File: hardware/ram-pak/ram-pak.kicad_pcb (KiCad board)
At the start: 4 copper layers, 29 x 16.7 mm, 29 parts, among them J1 PinHeader_2x22_P1.27mm, J2 pkl_jumper, U1 TLV62568DBV, U2 W957D8MFYA5I, U3 W957D8MFYA5I

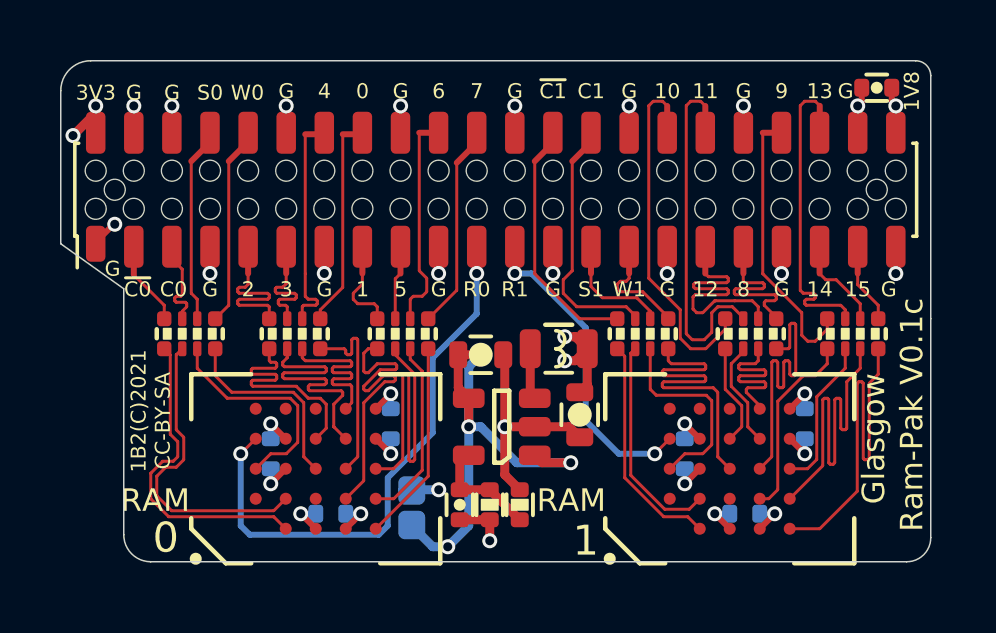
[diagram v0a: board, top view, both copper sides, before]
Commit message: Updated ram-pak files to KiCad V7.
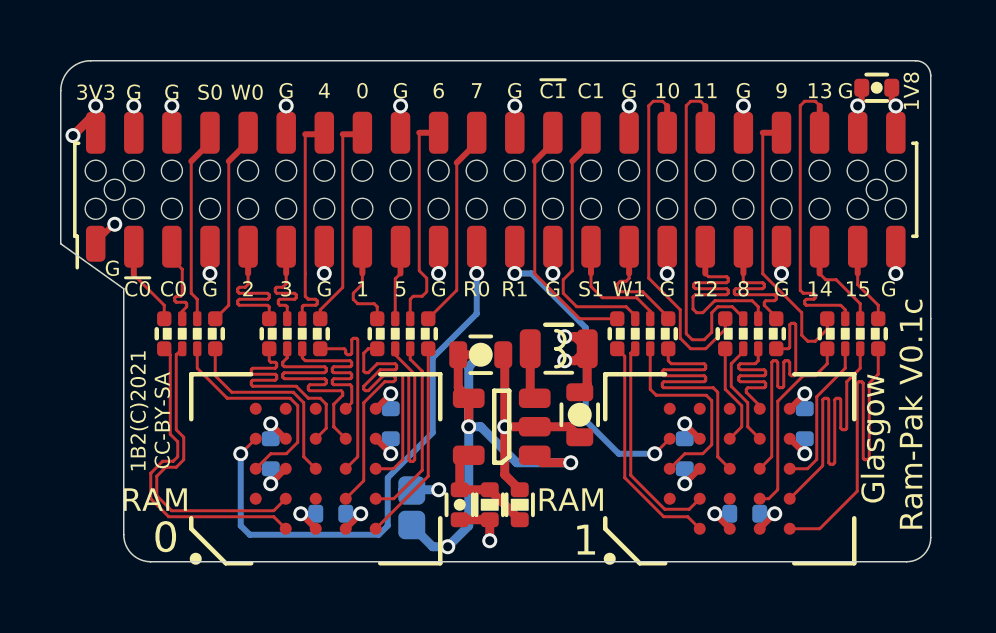
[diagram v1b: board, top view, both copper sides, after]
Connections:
- net /~CS0 renamed /~{CS0}
- net /~CS0x renamed /~{CS0x}
- net /~CS1 renamed /~{CS1}
- net /~CS1x renamed /~{CS1x}
- net /~RESET0 renamed /~{RESET0}
- net /~RESET1 renamed /~{RESET1}
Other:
- net class Default removed
- board text added: "~{C0}"
- board text added: "~{C1}"
- board text removed: "~C0"
- board text removed: "~C1"
